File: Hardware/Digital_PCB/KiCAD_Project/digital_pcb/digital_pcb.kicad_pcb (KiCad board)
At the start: 4 copper layers, 75 x 84.8 mm, 99 parts, among them J1 Conn_01x02, J2 ISP, J3 Conn_01x02, J4 Board to Board, J5 Spare 1, J6 Power, J7 Power Switch, Q1 MMBT3904, U1 STM32F103CBTx, U10 TPS793, U11 TPS1H000, U2 BNO055, U3 HTU21D, U4 ADS1220, U5 KC2520B-C2, U6 SN74LVC1G17-EP, U7 LT1521-3.3, U8 TEC 2-0921, U9 TPS723, Y1 8MHz, Y2 32.768kHz

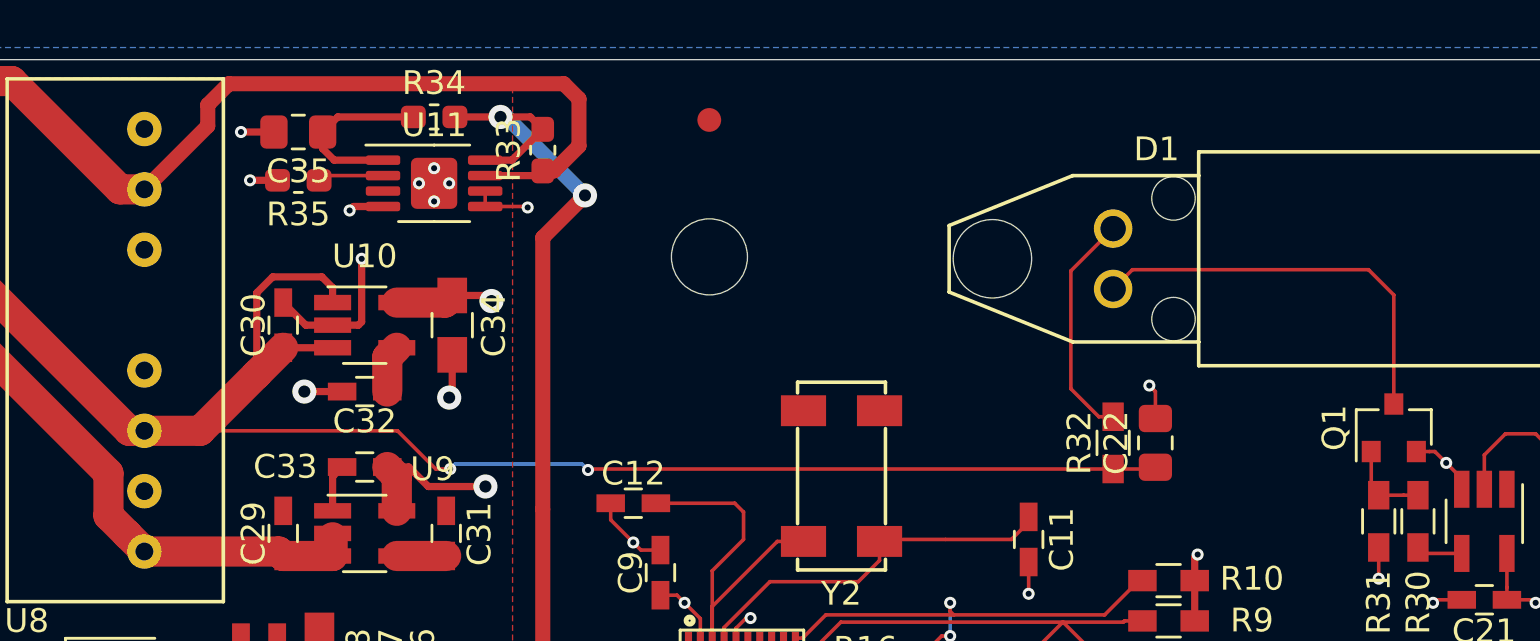
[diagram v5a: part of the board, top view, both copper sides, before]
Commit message: Update footprints for R32 and fix various small layout things and silk screen.
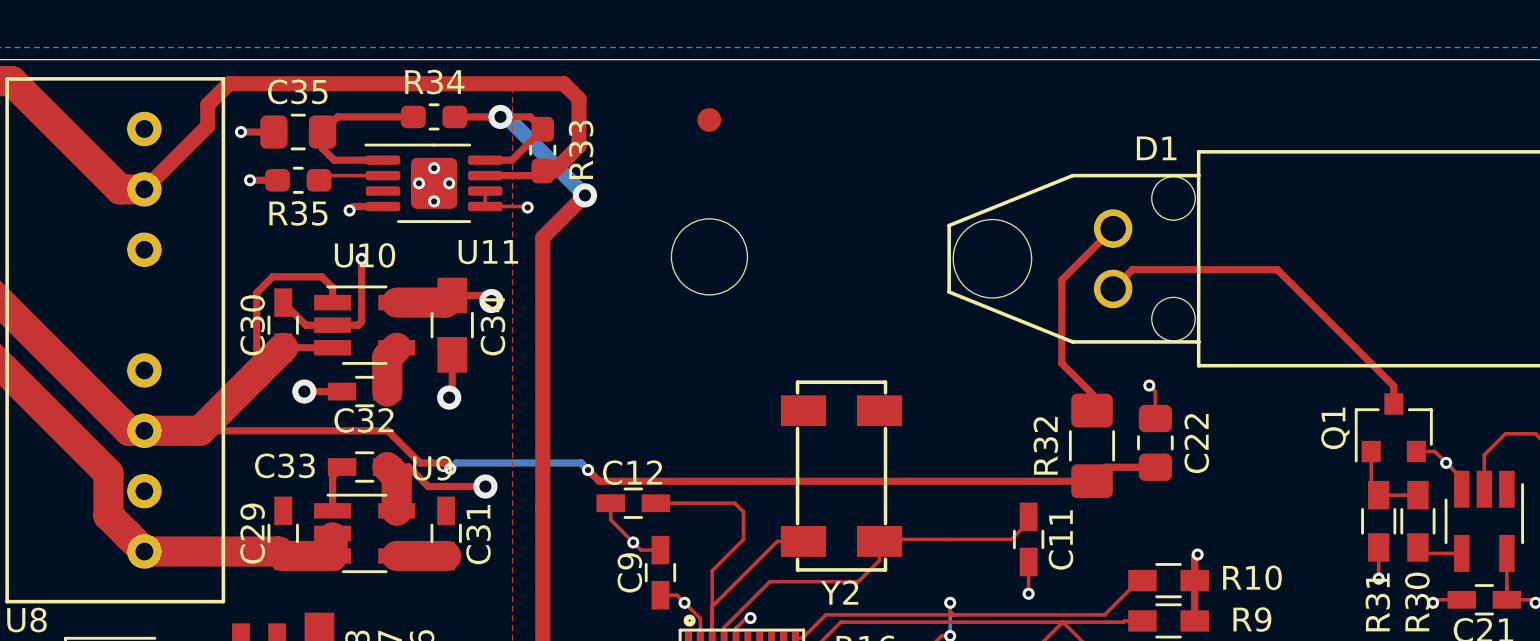
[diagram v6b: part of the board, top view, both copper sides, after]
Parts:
- R32: footprint Resistors_SMD:R_0603_HandSoldering -> Resistor_SMD:R_1206_3216Metric_Pad1.42x1.75mm_HandSolder
- moved R32 0.90 mm to (169.8, 70.1)
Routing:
- net Net-(D1-Pad1): track 17.2 -> 14.9 mm
- net +5V: track 76.1 -> 74.4 mm
- net Net-(D1-Pad2): track 9.74 -> 9.08 mm
